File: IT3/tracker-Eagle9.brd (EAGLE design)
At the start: 120 x 89.3 mm, 91 parts, among them J1 THING_PLUS_PHYSICAL, Q1 2N3906, Q2 DMG6602SVT, Q3 DMG6602SVT, Q6 MMBT3906LT1SMD, Q7 DMG6602SVT, U1 ADXL343BCCZ-RL7, U2 FONA-800-BREAKOUTNOHOLE, U3 MP2155GQ-Z, U4 SPARKFUN-SWARM-M138NOTOPHOLE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

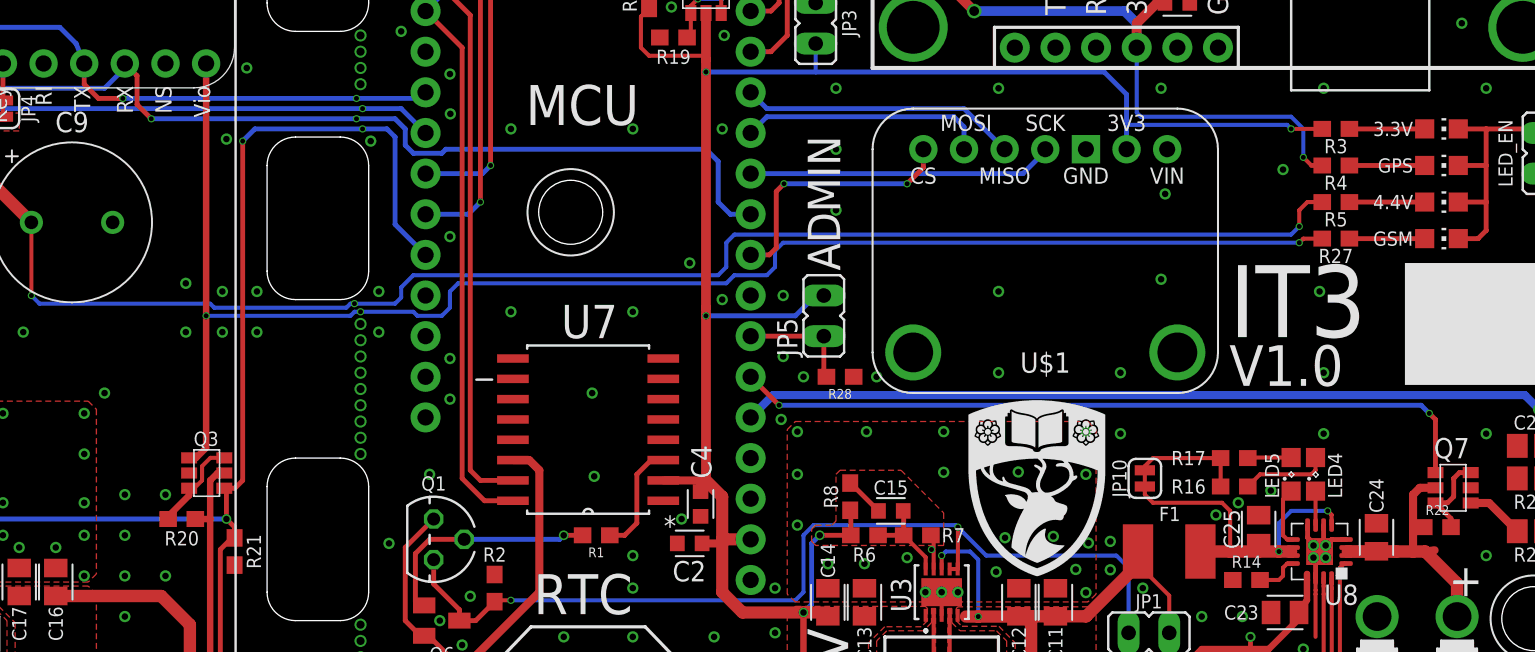
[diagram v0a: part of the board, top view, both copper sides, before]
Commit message: Firx DRC issues in Eagle 9
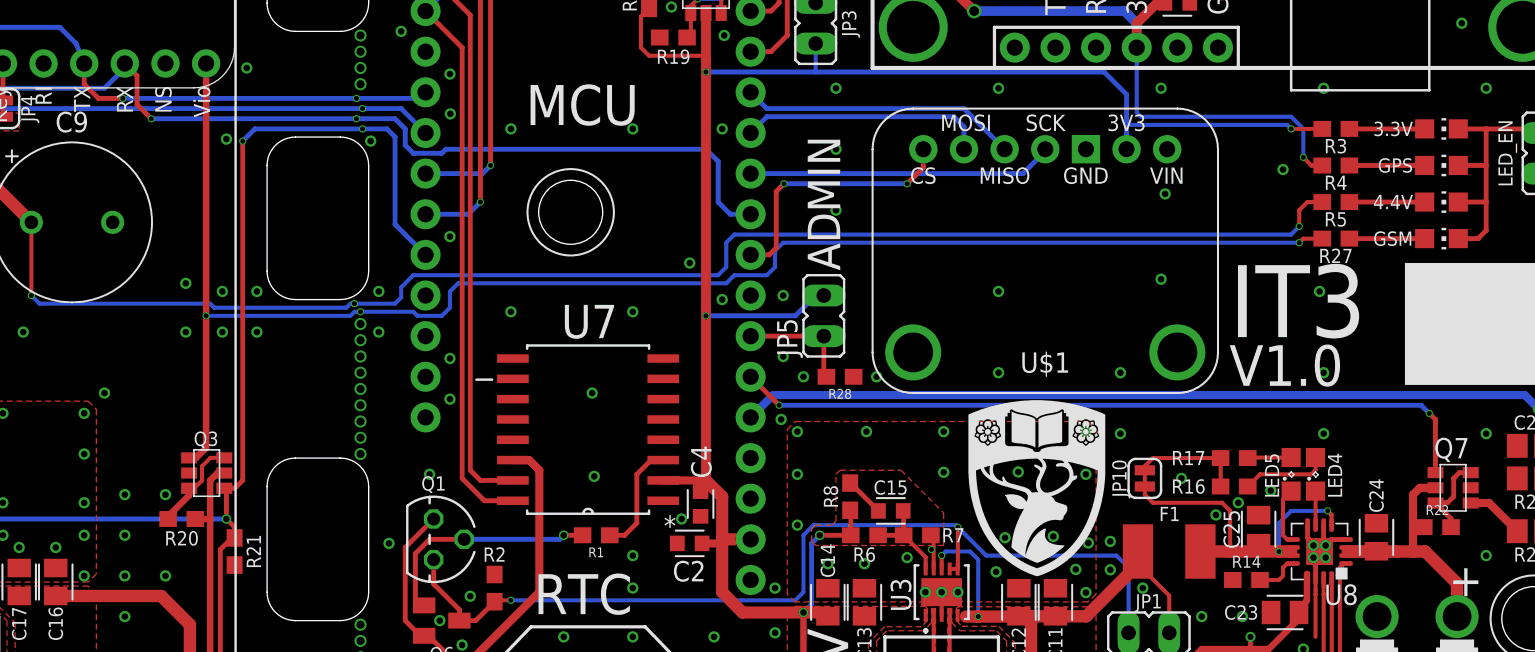
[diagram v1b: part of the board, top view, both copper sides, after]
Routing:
- net N$31: track 21.9 -> 22.9 mm
- net N$28: track 6.98 -> 8.00 mm
- net V_BATT: track 16.9 -> 16.3 mm
- net GND: vias 242 -> 243
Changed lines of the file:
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@@
 <grid distance="10" unitdist="mil" unit="mil" style="lines" multiple="1" display="yes" altdistance="5" altunitdist="mil" altunit="mil"/>
 <layers>
-<layer number="1" name="Top" color="4" fill="1" visible="no" active="yes"/>
+<layer number="1" name="Top" color="4" fill="1" visible="yes" active="yes"/>
 <layer number="2" name="Route2" color="16" fill="1" visible="no" active="no"/>
 <layer number="3" name="Route3" color="17" fill="1" visible="no" active="no"/>
@@
 <layer number="14" name="Route14" color="22" fill="1" visible="no" active="no"/>
 <layer number="15" name="Route15" color="23" fill="1" visible="no" active="no"/>
-<layer number="16" name="Bottom" color="1" fill="1" visible="yes" active="yes"/>
+<layer number="16" name="Bottom" color="1" fill="1" visible="no" active="yes"/>
 <layer number="17" name="Pads" color="2" fill="1" visible="yes" active="yes"/>
 <layer number="18" name="Vias" color="2" fill="1" visible="yes" active="yes"/>
 <layer number="19" name="Unrouted" color="6" fill="1" visible="yes" active="yes"/>
 <layer number="20" name="Dimension" color="24" fill="1" visible="yes" active="yes"/>
-<layer number="21" name="tPlace" color="7" fill="1" visible="no" active="yes"/>
-<layer number="22" name="bPlace" color="7" fill="1" visible="yes" active="yes"/>
-<layer number="23" name="tOrigins" color="15" fill="1" visible="no" active="yes"/>
-<layer number="24" name="bOrigins" color="15" fill="1" visible="yes" active="yes"/>
-<layer number="25" name="tNames" color="7" fill="1" visible="no" active="yes"/>
-<layer number="26" name="bNames" color="7" fill="1" visible="yes" active="yes"/>
+<layer number="21" name="tPlace" color="7" fill="1" visible="yes" active="yes"/>
+<layer number="22" name="bPlace" color="7" fill="1" visible="no" active="yes"/>
+<layer number="23" name="tOrigins" color="15" fill="1" visible="yes" active="yes"/>
+<layer number="24" name="bOrigins" color="15" fill="1" visible="no" active="yes"/>
+<layer number="25" name="tNames" color="7" fill="1" visible="yes" active="yes"/>
+<layer number="26" name="bNames" color="7" fill="1" visible="no" active="yes"/>
 <layer number="27" name="tValues" color="7" fill="1" visible="no" active="yes"/>
 <layer number="28" name="bValues" color="7" fill="1" visible="no" active="yes"/>
@@
 <layer number="37" name="tTest" color="7" fill="1" visible="no" active="yes"/>
 <layer number="38" name="bTest" color="7" fill="1" visible="no" active="yes"/>
-<layer number="39" name="tKeepout" color="4" fill="11" visible="no" active="yes"/>
-<layer number="40" name="bKeepout" color="1" fill="11" visible="yes" active="yes"/>
-<layer number="41" name="tRestrict" color="4" fill="10" visible="no" active="yes"/>
-<layer number="42" name="bRestrict" color="1" fill="10" visible="yes" active="yes"/>
+<layer number="39" name="tKeepout" color="4" fill="11" visible="yes" active="yes"/>
+<layer number="40" name="bKeepout" color="1" fill="11" visible="no" active="yes"/>
+<layer number="41" name="tRestrict" color="4" fill="10" visible="yes" active="yes"/>
+<layer number="42" name="bRestrict" color="1" fill="10" visible="no" active="yes"/>
 <layer number="43" name="vRestrict" color="2" fill="10" visible="no" active="yes"/>
-<layer number="44" name="Drills" color="7" fill="1" visible="yes" active="yes"/>
-<layer number="45" name="Holes" color="7" fill="1" visible="yes" active="yes"/>
-<layer number="46" name="Milling" color="3" fill="1" visible="yes" active="yes"/>
+<layer number="44" name="Drills" color="7" fill="1" visible="no" active="yes"/>
+<layer number="45" name="Holes" color="7" fill="1" visible="no" active="yes"/>
+<layer number="46" name="Milling" color="3" fill="1" visible="no" active="yes"/>
 <layer number="47" name="Measures" color="7" fill="1" visible="no" active="yes"/>
 <layer number="48" name="Document" color="7" fill="1" visible="no" active="yes"/>
 <layer number="49" name="Reference" color="7" fill="1" visible="no" active="yes"/>
 <layer number="50" name="dxf" color="7" fill="1" visible="no" active="no"/>
-<layer number="51" name="tDocu" color="7" fill="1" visible="no" active="yes"/>
-<layer number="52" name="bDocu" color="7" fill="1" visible="yes" active="yes"/>
+<layer number="51" name="tDocu" color="7" fill="1" visible="yes" active="yes"/>
+<layer number="52" name="bDocu" color="7" fill="1" visible="no" active="yes"/>
 <layer number="53" name="tGND_GNDA" color="7" fill="9" visible="no" active="no"/>
 <layer number="54" name="bGND_GNDA" color="1" fill="9" visible="no" active="no"/>
@@
 <layer number="196" name="mValues" color="7" fill="1" visible="no" active="no"/>
 <layer number="199" name="Contour" color="7" fill="1" visible="no" active="no"/>
-<layer number="200" name="200bmp" color="1" fill="10" visible="yes" active="yes"/>
+<layer number="200" name="200bmp" color="1" fill="10" visible="no" active="yes"/>
 <layer number="201" name="201bmp" color="2" fill="10" visible="no" active="no"/>
 <layer number="202" name="202bmp" color="3" fill="10" visible="no" active="no"/>
@@
 <via x="70.358" y="27.686" extent="1-16" drill="0.4064" diameter="0.7112"/>
 <via x="70.358" y="31.496" extent="1-16" drill="0.4064" diameter="0.7112"/>
+<via x="95.25" y="20.066" extent="1-16" drill="0.4064" diameter="0.7112"/>
 </signal>
 <signal name="GPS_RX2">
@@
 <wire x1="70.104" y1="49.784" x2="69.596" y2="49.276" width="0.3048" layer="1"/>
 <wire x1="68.326" y1="49.276" x2="69.596" y2="49.276" width="0.3048" layer="1"/>
-<wire x1="72.898" y1="54.356" x2="89.916" y2="46.99" width="0" layer="19" extent="1-1"/>
+<wire x1="68.326" y1="49.276" x2="89.916" y2="46.99" width="0" layer="19" extent="1-1"/>
 </signal>
 <signal name="GPS_TX2">
@@
 <wire x1="70.612" y1="47.752" x2="69.596" y2="46.736" width="0.3048" layer="1"/>
 <wire x1="69.596" y1="46.736" x2="68.326" y2="46.736" width="0.3048" layer="1"/>
-<wire x1="73.406" y1="54.102" x2="87.376" y2="46.99" width="0" layer="19" extent="1-1"/>
+<wire x1="68.326" y1="46.736" x2="87.376" y2="46.99" width="0" layer="19" extent="1-1"/>
 </signal>
 <signal name="3.3V">
@@
 <wire x1="115.31" y1="56.356" x2="115.31" y2="58.553" width="0.3048" layer="1"/>
 <wire x1="115.31" y1="58.553" x2="114.554" y2="59.309" width="0.3048" layer="1"/>
-<wire x1="50.038" y1="57.658" x2="77.216" y2="72.39" width="0" layer="19" extent="16-16"/>
+<wire x1="48.006" y1="51.816" x2="77.216" y2="72.39" width="0" layer="19" extent="1-1"/>
 </signal>
 <signal name="SCL">
@@
 <wire x1="114.3" y1="56.366" x2="114.3" y2="57.277" width="0.3048" layer="1"/>
 <wire x1="114.3" y1="57.277" x2="113.919" y2="57.658" width="0.3048" layer="1"/>
-<wire x1="50.292" y1="57.023" x2="77.216" y2="80.01" width="0" layer="19" extent="16-16"/>
+<wire x1="48.006" y1="49.276" x2="77.216" y2="80.01" width="0" layer="19" extent="1-1"/>
 </signal>
 <signal name="COMMS_RX">
@@
 <wire x1="47.625" y1="43.815" x2="43.688" y2="43.815" width="0.3048" layer="16"/>
 <wire x1="43.688" y1="43.815" x2="29.083" y2="43.815" width="0.3048" layer="16"/>
-<wire x1="28.829" y1="43.815" x2="29.083" y2="43.815" width="0.3048" layer="1"/>
 <wire x1="26.67" y1="45.974" x2="26.67" y2="44.704" width="0.3048" layer="1"/>
 <wire x1="26.67" y1="44.704" x2="27.559" y2="43.815" width="0.3048" layer="1"/>
-<wire x1="27.559" y1="43.815" x2="29.083" y2="43.815" width="0.3048" layer="1"/>
+<wire x1="29.083" y1="43.815" x2="27.559" y2="43.815" width="0.3048" layer="1"/>
 <wire x1="26.67" y1="45.9994" x2="26.67" y2="45.974" width="0.6096" layer="1"/>
 <via x="43.688" y="43.815" extent="1-16" drill="0.3048"/>
@@
 <wire x1="47.922" y1="10.226" x2="48.202" y2="10.226" width="0.3048" layer="1"/>
 <wire x1="48.202" y1="10.226" x2="50.296" y2="8.132" width="0.3048" layer="1"/>
-<wire x1="55.118" y1="12.954" x2="66.036" y2="4.064" width="0" layer="19" extent="1-1"/>
+<wire x1="50.296" y1="4.064" x2="66.036" y2="4.064" width="0" layer="19" extent="1-1"/>
 </signal>
 <signal name="GSM_RST">
@@
 <contactref element="Q7" pad="P$2"/>
 <contactref element="R22" pad="1"/>
-<wire x1="111.078" y1="15.574" x2="110.49" y2="15.494" width="0.508" layer="1"/>
 <wire x1="111.13" y1="19.478" x2="110.156" y2="19.478" width="0.508" layer="1"/>
 <wire x1="110.156" y1="19.478" x2="109.728" y2="19.05" width="0.508" layer="1"/>
@@
 <wire x1="97.702" y1="21.336" x2="93.472" y2="21.336" width="0.254" layer="1"/>
 <wire x1="92.964" y1="20.828" x2="93.472" y2="21.336" width="0.254" layer="1"/>
-<wire x1="92.964" y1="20.828" x2="92.964" y2="20.574" width="0.254" layer="1"/>
+<wire x1="92.964" y1="20.574" x2="92.964" y2="20.828" width="0.254" layer="1"/>
+<wire x1="92.964" y1="19.558" x2="92.964" y2="20.574" width="0.1524" layer="1"/>
 </signal>
 <signal name="N$29">
@@
 <wire x1="101.346" y1="17.272" x2="101.346" y2="15.494" width="0.254" layer="16"/>
 <via x="101.346" y="15.494" extent="1-16" drill="0.3048"/>
+<wire x1="92.964" y1="20.574" x2="92.964" y2="19.558" width="0.1524" layer="1"/>
 </signal>
 <signal name="GPS_EN">
